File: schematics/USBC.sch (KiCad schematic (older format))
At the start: 3 parts, among them J3 USB_C_Receptacle

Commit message: feat: external power circuit schematics
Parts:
- J3: symbol Connector:USB_C_Receptacle -> PSLab:USB_C_Receptacle
- R59, R60: value 5k1 -> 5K1
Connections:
- no-connect marks 10 -> 2
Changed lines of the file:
@@
 $EndDescr
 $Comp
-L Connector:USB_C_Receptacle J3
+L PSLab:USB_C_Receptacle J3
 U 1 1 5ED26D9E
 P 6150 2625
@@
 P 6850 4150
 F 0 "R59" H 6920 4196 50  0000 L CNN
-F 1 "5k1" H 6920 4105 50  0000 L CNN
+F 1 "5K1" H 6920 4105 50  0000 L CNN
 F 2 "Resistor_SMD:R_0603_1608Metric" V 6780 4150 50  0001 C CNN
 F 3 "~" H 6850 4150 50  0001 C CNN
@@
 P 7150 4150
 F 0 "R60" H 7220 4196 50  0000 L CNN
-F 1 "5k1" H 7220 4105 50  0000 L CNN
+F 1 "5K1" H 7220 4105 50  0000 L CNN
 F 2 "Resistor_SMD:R_0603_1608Metric" V 7080 4150 50  0001 C CNN
 F 3 "~" H 7150 4150 50  0001 C CNN
@@
 NoConn ~ 4850 3225
 NoConn ~ 4950 3225
-NoConn ~ 5150 3225
-NoConn ~ 5250 3225
-NoConn ~ 5450 3225
-NoConn ~ 5550 3225
-NoConn ~ 5750 3225
-NoConn ~ 5850 3225
-NoConn ~ 6050 3225
-NoConn ~ 6150 3225
 Text HLabel 8050 3300 2    60   Output ~ 0
 VBus

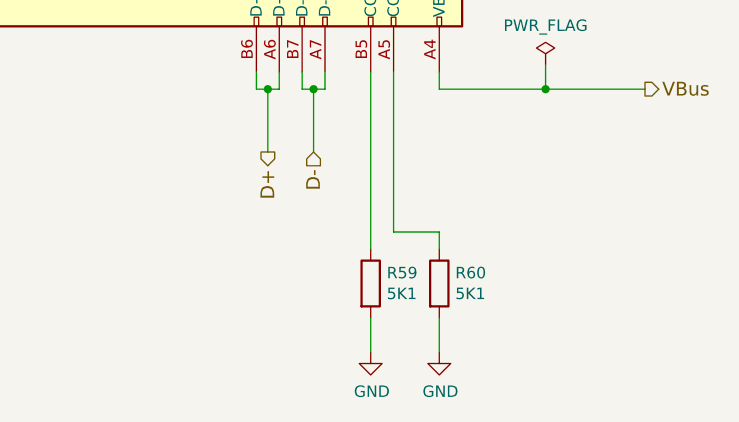
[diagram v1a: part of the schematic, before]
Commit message: refactor: fixed rotation in resistors
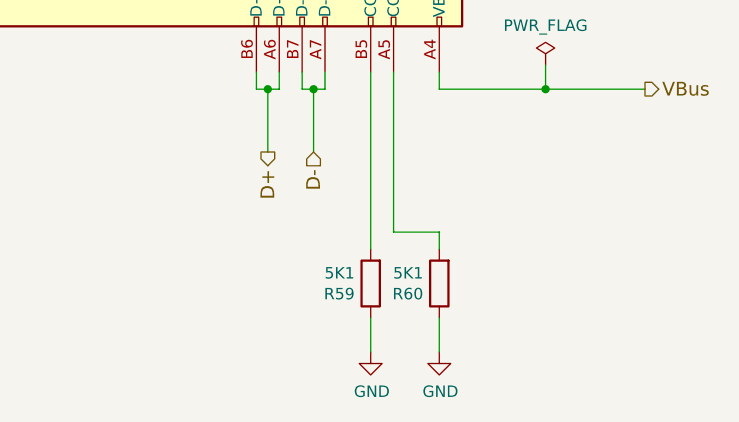
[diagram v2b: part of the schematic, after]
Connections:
- net GND: now also R59.1, R60.1; no longer R59.2, R60.2
- net at J3.A5 (CC1): now also R60.2; no longer R60.1
- net at J3.B5 (CC2): now also R59.2; no longer R59.1
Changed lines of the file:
@@
 F 3 "~" H 6850 4150 50  0001 C CNN
 	1    6850 4150
-	1    0    0    -1
+	-1   0    0    1
 $EndComp
 $Comp
@@
 F 3 "~" H 7150 4150 50  0001 C CNN
 	1    7150 4150
-	1    0    0    -1
+	-1   0    0    1
 $EndComp
 Wire Wire Line

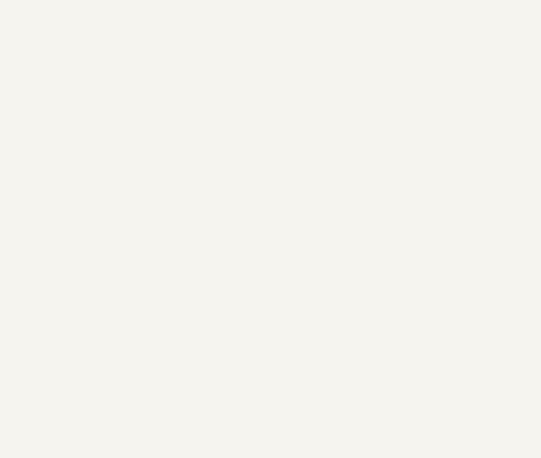
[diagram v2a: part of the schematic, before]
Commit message: feat: enhanced bottom silk screen
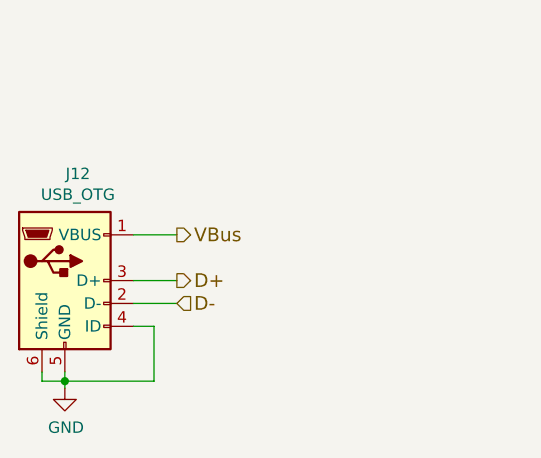
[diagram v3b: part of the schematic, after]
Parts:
- added J12: USB_OTG, Connector_USB:USB_Micro-B_Molex_47346-0001, symbol Connector:USB_OTG
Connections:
- net D+: now also J12.3 (D+)
- net D-: now also J12.2 (D-)
- net GND: now also J12.4 (ID), J12.5 (GND), J12.6 (Shield)
- net VBus: now also J12.1 (VBUS)
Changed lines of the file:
@@
 Wire Wire Line
 	7615 3300 7150 3300
+$Comp
+L Connector:USB_OTG J12
+U 1 1 5F908415
+P 2490 4810
+F 0 "J12" H 2547 5277 50  0000 C CNN
+F 1 "USB_OTG" H 2547 5186 50  0000 C CNN
+F 2 "Connector_USB:USB_Micro-B_Molex_47346-0001" H 2640 4760 50  0001 C CNN
+F 3 " ~" H 2640 4760 50  0001 C CNN
+	1    2490 4810
+	1    0    0    -1
+$EndComp
+$Comp
+L power:GND #PWR034
+U 1 1 5F909117
+P 2490 5280
+F 0 "#PWR034" H 2490 5030 50  0001 C CNN
+F 1 "GND" H 2495 5107 50  0000 C CNN
+F 2 "" H 2490 5280 50  0001 C CNN
+F 3 "" H 2490 5280 50  0001 C CNN
+	1    2490 5280
+	1    0    0    -1
+$EndComp
+Wire Wire Line
+	2490 5280 2490 5250
+Wire Wire Line
+	2390 5210 2390 5250
+Wire Wire Line
+	2390 5250 2490 5250
+Connection ~ 2490 5250
+Wire Wire Line
+	2490 5250 2490 5210
+Text HLabel 2980 4810 2    60   Output ~ 0
+D+
+Wire Wire Line
+	2980 4810 2790 4810
+Text HLabel 2980 4910 2    60   Input ~ 0
+D-
+Wire Wire Line
+	2790 4910 2980 4910
+Wire Wire Line
+	2790 5010 2880 5010
+Wire Wire Line
+	2880 5010 2880 5250
+Wire Wire Line
+	2880 5250 2490 5250
+Text HLabel 2980 4610 2    60   Output ~ 0
+VBus
+Wire Wire Line
+	2980 4610 2790 4610
 $EndSCHEMATC

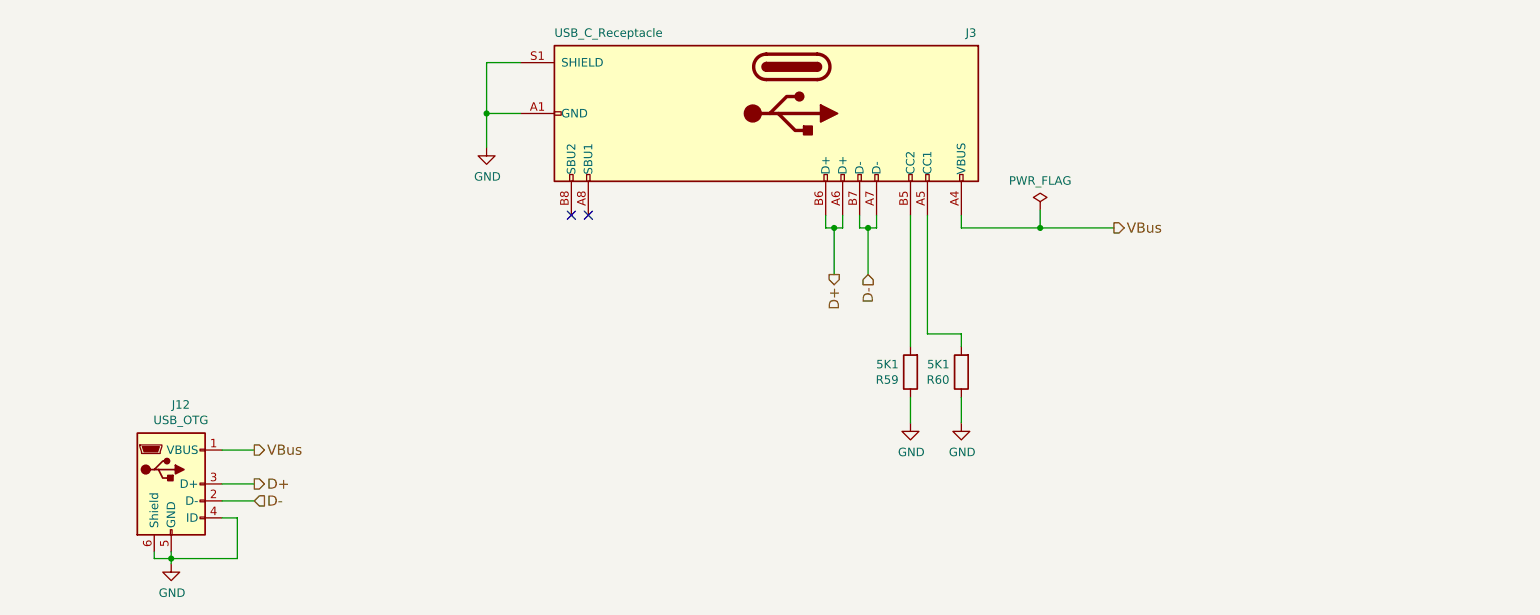
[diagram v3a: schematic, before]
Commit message: feat: bom generator and updated project to support bom generator
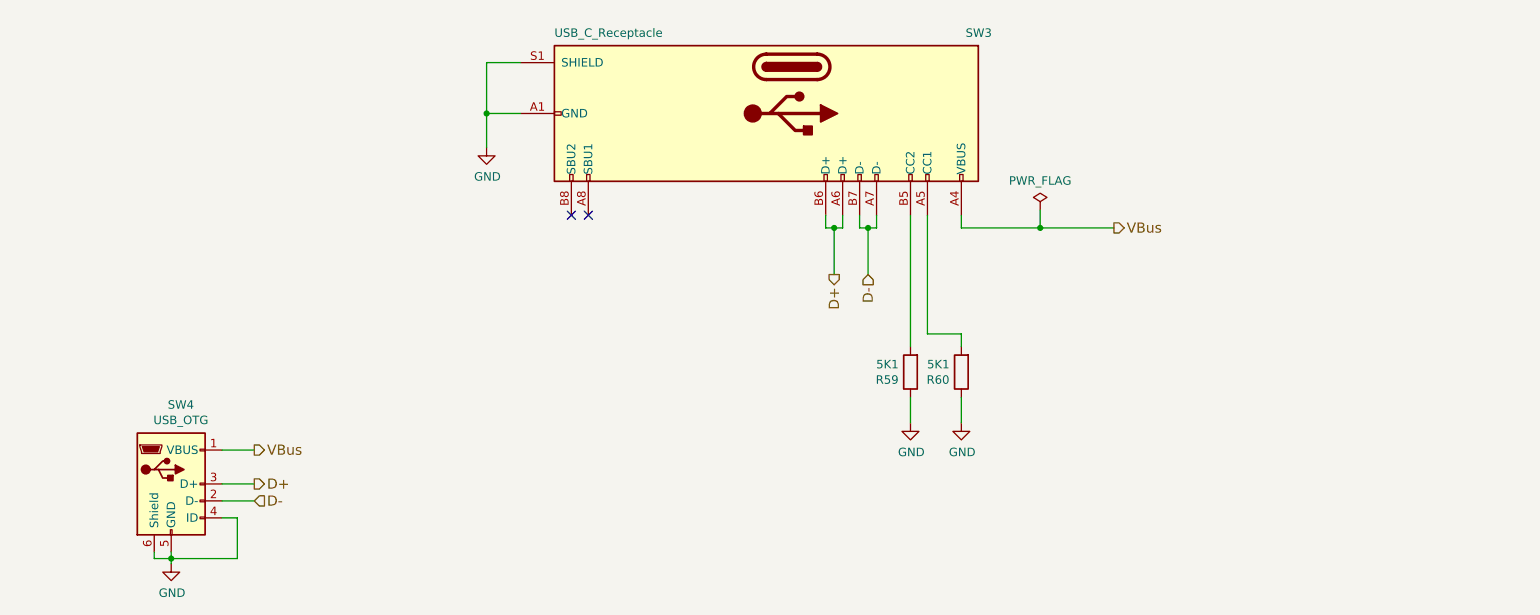
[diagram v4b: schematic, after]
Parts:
- R59, R60: Description (none) -> 1/16W 5%; Mfr No. (none) -> RR0816P-512-D; PartNumber (none) -> RR0816P-512-D; Price (none) -> 0.1
- SW3: renamed from J3; Description (none) -> USB - Type C Female 16 SMT; Mfr No. (none) -> U262-161N-4BVC11; PartNumber (none) -> U262-161N-4BVC11; Price (none) -> 0.32
- SW4: renamed from J12; Description (none) -> USB - Micro B Recepticle Molex; Mfr No. (none) -> 47346-0001; PartNumber (none) -> 47346-0001; Price (none) -> 0.81
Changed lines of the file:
@@
 $EndDescr
 $Comp
-L PSLab:USB_C_Receptacle J3
+L PSLab:USB_C_Receptacle SW3
 U 1 1 5ED26D9E
 P 6150 2625
-F 0 "J3" V 5675 3650 50  0000 L CNN
+F 0 "SW3" V 5675 3650 50  0000 L CNN
 F 1 "USB_C_Receptacle" V 5675 1225 50  0000 L CNN
 F 2 "Connector_USB:USB_C_Receptacle_XKB_U262-16XN-4BVC11" H 6300 2625 50  0001 C CNN
 F 3 "https://www.usb.org/sites/default/files/documents/usb_type-c.zip" H 6300 2625 50  0001 C CNN
+F 4 "USB - Type C Female 16 SMT" H 6150 2625 50  0001 C CNN "Description"
+F 5 "U262-161N-4BVC11" H 6150 2625 50  0001 C CNN "Mfr No."
+F 6 "U262-161N-4BVC11" H 6150 2625 50  0001 C CNN "PartNumber"
+F 7 "0.32" H 6150 2625 50  0001 C CNN "Price"
 	1    6150 2625
 	0    1    1    0
@@
 F 1 "5K1" H 6920 4105 50  0000 L CNN
 F 2 "Resistor_SMD:R_0603_1608Metric" V 6780 4150 50  0001 C CNN
-F 3 "~" H 6850 4150 50  0001 C CNN
+F 3 "https://eu.mouser.com/datasheet/2/392/susumu_RR_Data_Sheet-1206438.pdf" H 6850 4150 50  0001 C CNN
+F 4 "1/16W 5%" H 6850 4150 50  0001 C CNN "Description"
+F 5 "RR0816P-512-D" H 6850 4150 50  0001 C CNN "Mfr No."
+F 6 "0.1" H 6850 4150 50  0001 C CNN "Price"
+F 7 "RR0816P-512-D" H 6850 4150 50  0001 C CNN "PartNumber"
 	1    6850 4150
 	-1   0    0    1
@@
 F 1 "5K1" H 7220 4105 50  0000 L CNN
 F 2 "Resistor_SMD:R_0603_1608Metric" V 7080 4150 50  0001 C CNN
-F 3 "~" H 7150 4150 50  0001 C CNN
+F 3 "https://eu.mouser.com/datasheet/2/392/susumu_RR_Data_Sheet-1206438.pdf" H 7150 4150 50  0001 C CNN
+F 4 "1/16W 5%" H 7150 4150 50  0001 C CNN "Description"
+F 5 "RR0816P-512-D" H 7150 4150 50  0001 C CNN "Mfr No."
+F 6 "0.1" H 7150 4150 50  0001 C CNN "Price"
+F 7 "RR0816P-512-D" H 7150 4150 50  0001 C CNN "PartNumber"
 	1    7150 4150
 	-1   0    0    1
@@
 	7615 3300 7150 3300
 $Comp
-L Connector:USB_OTG J12
+L Connector:USB_OTG SW4
 U 1 1 5F908415
 P 2490 4810
-F 0 "J12" H 2547 5277 50  0000 C CNN
+F 0 "SW4" H 2547 5277 50  0000 C CNN
 F 1 "USB_OTG" H 2547 5186 50  0000 C CNN
 F 2 "Connector_USB:USB_Micro-B_Molex_47346-0001" H 2640 4760 50  0001 C CNN
-F 3 " ~" H 2640 4760 50  0001 C CNN
+F 3 "https://www.mouser.fi/datasheet/2/276/0473460001_IO_CONNECTORS-229243.pdf" H 2640 4760 50  0001 C CNN
+F 4 "USB - Micro B Recepticle Molex" H 2490 4810 50  0001 C CNN "Description"
+F 5 "47346-0001" H 2490 4810 50  0001 C CNN "Mfr No."
+F 6 "47346-0001" H 2490 4810 50  0001 C CNN "PartNumber"
+F 7 "0.81" H 2490 4810 50  0001 C CNN "Price"
 	1    2490 4810
 	1    0    0    -1

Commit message: fix: USB C at bottom, gerber files in .gbr
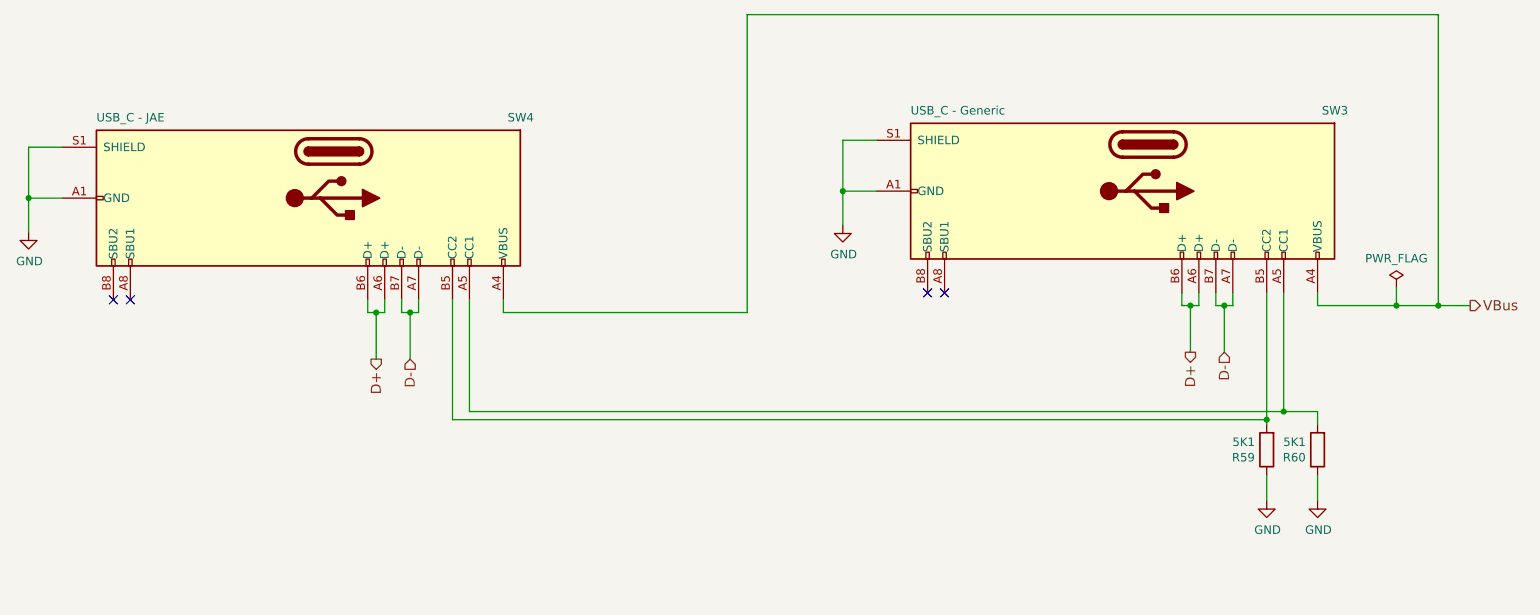
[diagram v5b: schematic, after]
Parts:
- removed SW4: USB_OTG, Connector_USB:USB_Micro-B_Molex_47346-0001, symbol Connector:USB_OTG
- added SW4: USB_C - JAE, Connector_USB:USB_C_Receptacle_XKB_U262-16XN-4BVC11, symbol PSLab:USB_C_Receptacle
- SW3: value USB_C_Receptacle -> USB_C - Generic
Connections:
- net D+: now also SW4.A6 (D+), SW4.B6 (D+)
- net D-: now also SW4.A7 (D-), SW4.B7 (D-)
- net GND: now also SW4.A1 (GND), SW4.A12 (GND), SW4.B1 (GND), SW4.B12 (GND), SW4.S1 (SHIELD)
- net VBus: now also SW4.A4 (VBUS), SW4.A9 (VBUS), SW4.B4 (VBUS), SW4.B9 (VBUS)
- net at R60.2, SW3.A5 (CC1): now also SW4.A5 (CC1)
- net at R59.2, SW3.B5 (CC2): now also SW4.B5 (CC2)
- no-connect marks 2 -> 4
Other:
- moved on the sheet: R59, R60, SW3
